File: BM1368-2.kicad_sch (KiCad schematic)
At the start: 39 parts, among them U11 BM1370_mode1, U12 BM1370_mode1

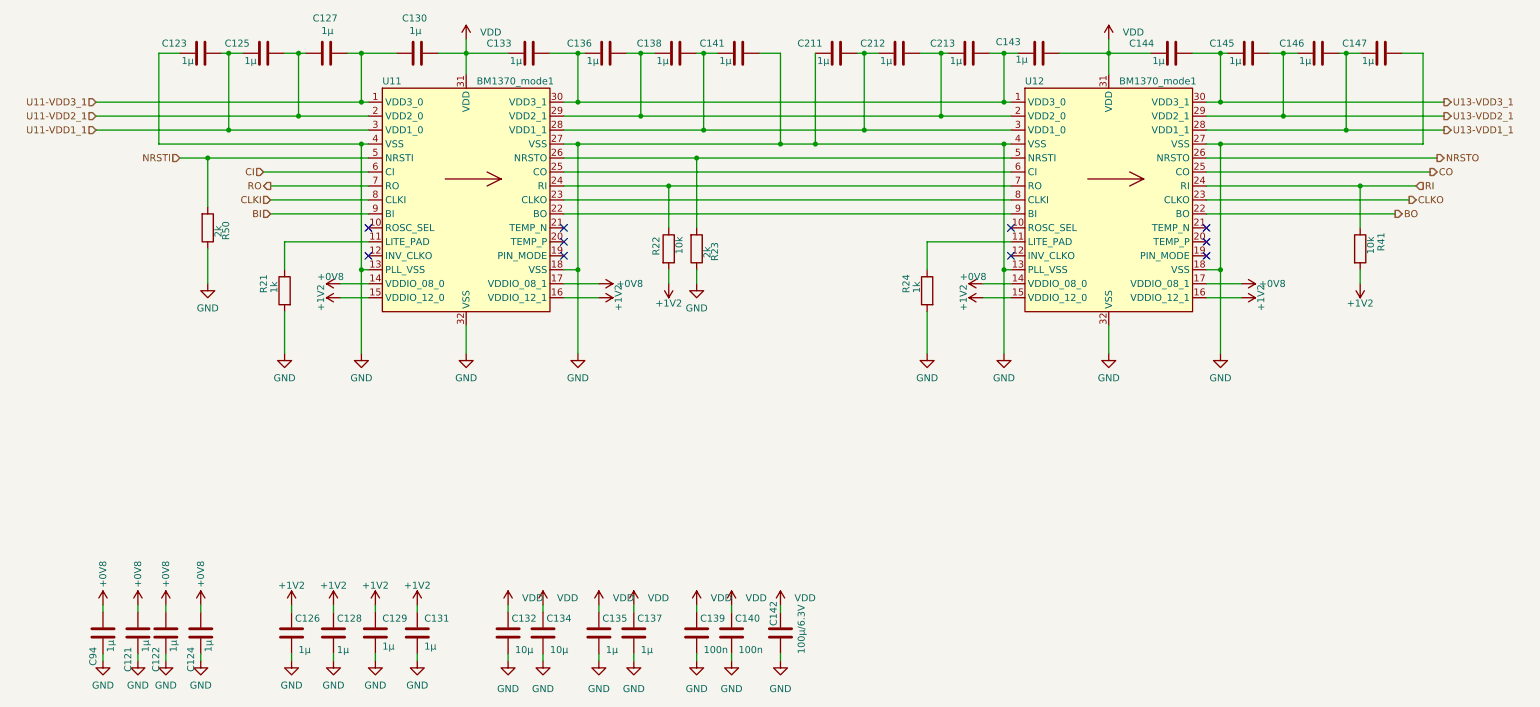
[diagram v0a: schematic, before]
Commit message: BOM changes
1nF  to 1nF 0.7mm etc
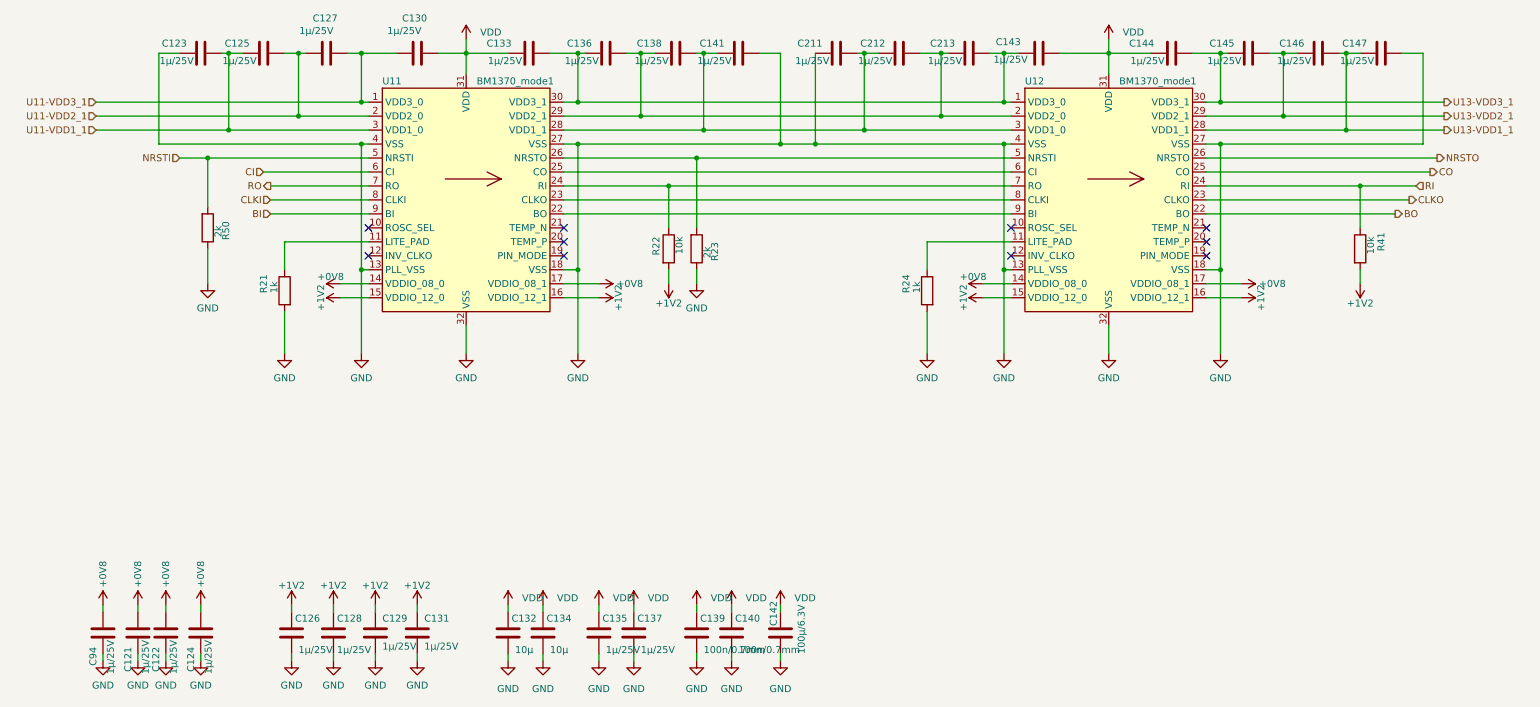
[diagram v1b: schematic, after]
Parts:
- C121, C122, C123, C124, C125, C126, C127, C128, C129, C130, C131, C133, C135, C136, C137, C138, C141, C143, C144, C145, C146, C147, C211, C212, C213, C94: value 1µ -> 1µ/25V; Distributor (none) -> D; Manufacturer (none) -> CL21B105KAFNNNE; OrderNr (none) -> 1276-1066-1-ND
- C139, C140: value 100n -> 100n/0.7mm; Distributor (none) -> D; Manufacturer (none) -> AC0805KRX7R9BB104; OrderNr (none) -> 311-3037-1-ND
- R21, R24: Distributor (none) -> D; Manufacturer (none) -> RNCP0805FTD1K00; OrderNr (none) -> RNCP0805FTD1K00CT-ND
- R22, R41: Distributor (none) -> D; Manufacturer (none) -> RMCF0805FT10K0; OrderNr (none) -> RMCF0805FT10K0CT-ND
- R23, R50: Distributor (none) -> D; Manufacturer (none) -> CRG0805F2K0; OrderNr (none) -> A126358CT-ND
- U11, U12: Manufacturer (none) -> BM1370 BITMAIN; OrderNr (none) -> -
